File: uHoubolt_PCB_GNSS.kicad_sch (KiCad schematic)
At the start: 88 parts, among them J1 Power In, J12 MMCX-J-P-H-RA-SM1, J2 Debug, J3 Debug, J4 CAN1, J5 CAN2, J6 CAN1, J7 CAN2, Q1 SISA88DN or similar, U1 SAM-M8Q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

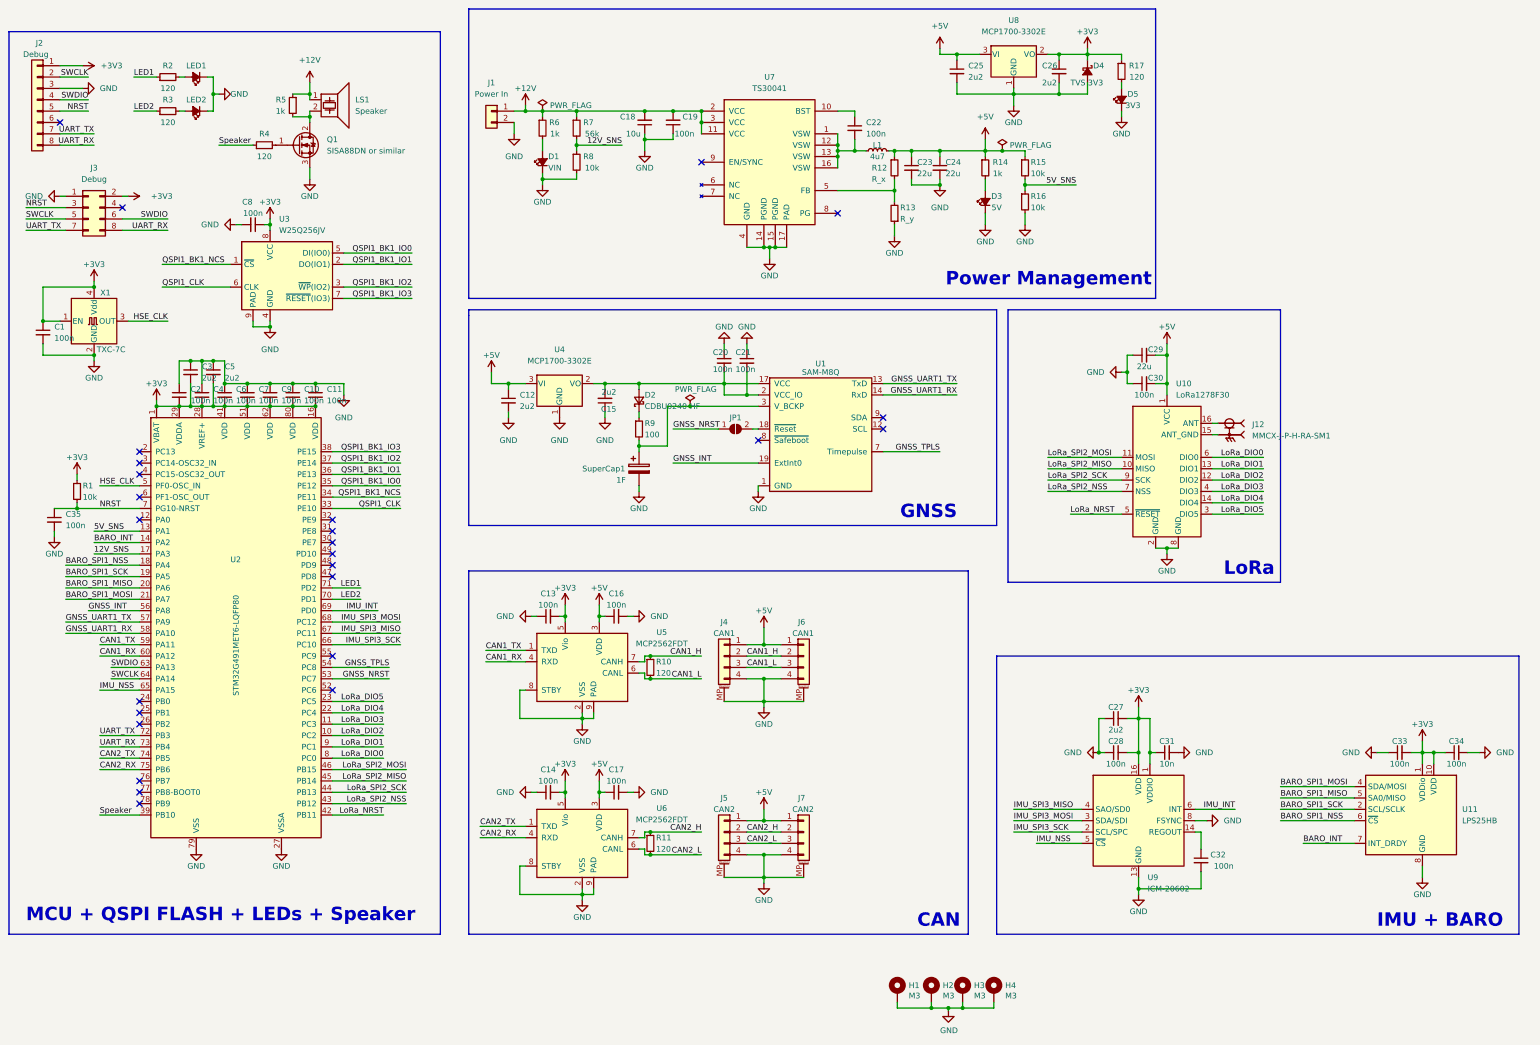
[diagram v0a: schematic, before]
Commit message: Rounded board; updated LoRa module; Small bugfixes and rewiring
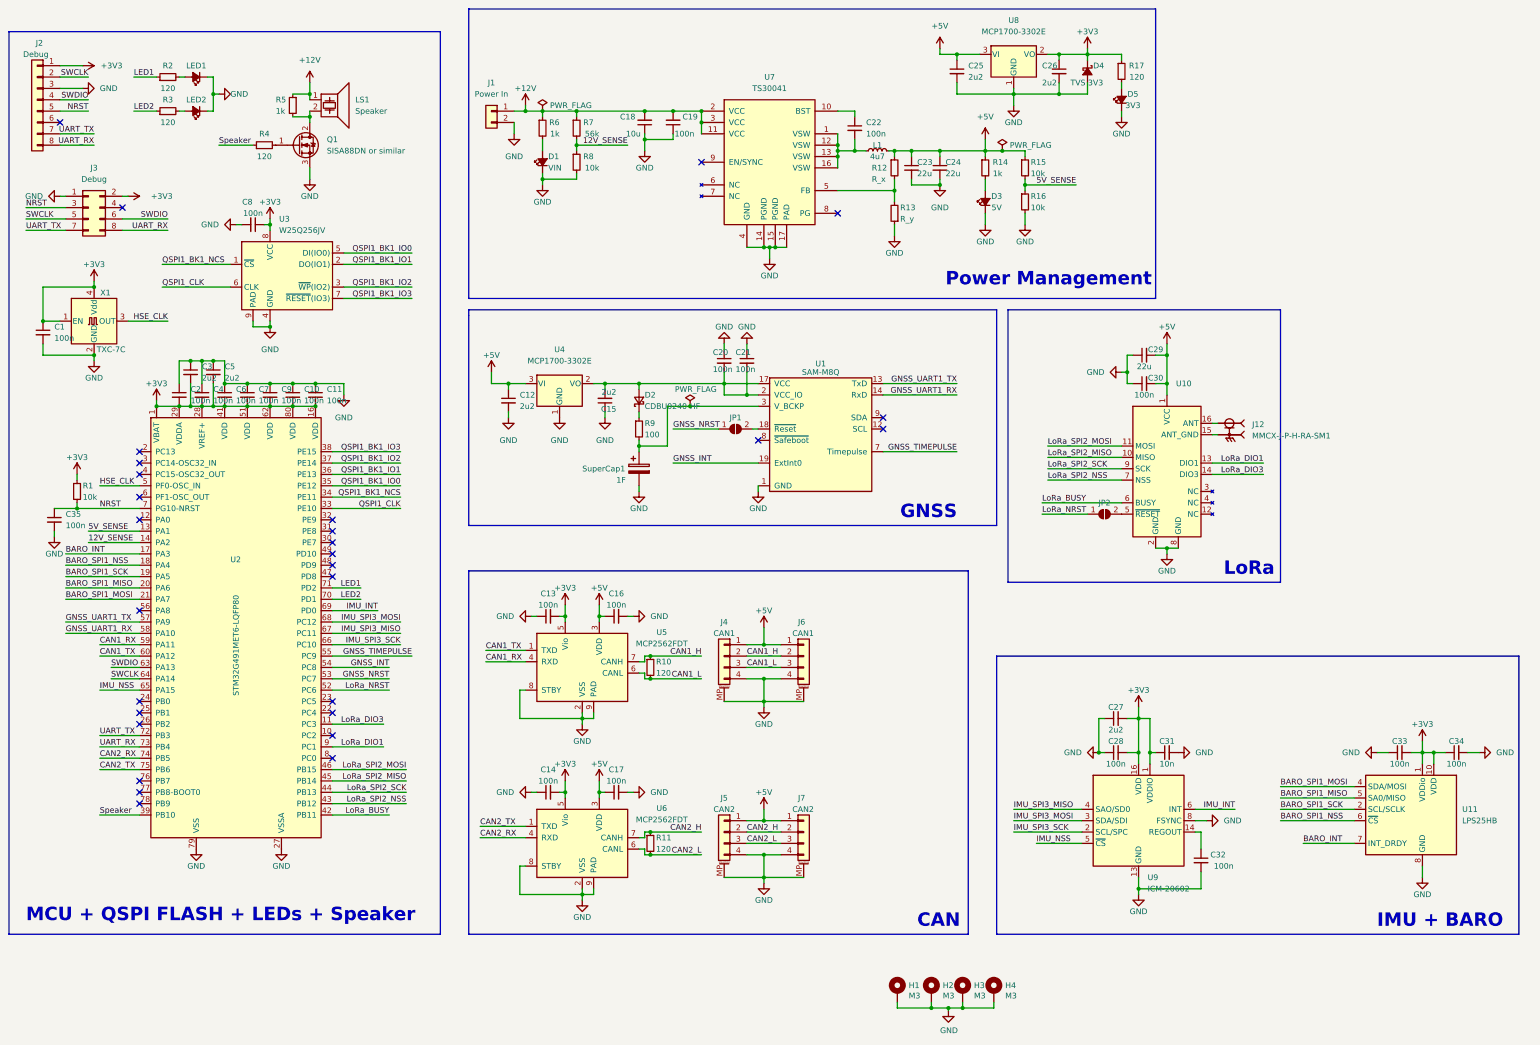
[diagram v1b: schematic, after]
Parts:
- removed U10: LoRa1278F30, TXV_Library_Footprints:G-NiceRF-LoRa1278F30, symbol TXV_Library_Symbols:LoRa1278F30
- added JP2: (no value), symbol Jumper:SolderJumper_2_Open
- added U10: (no value), symbol TXV_Library_Symbols:LoRa1276F30
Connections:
- net +5V: now also U10.1 (VCC)
- net BARO_INT: now also U2.17 (PA3); no longer U2.14 (PA2)
- net CAN1_RX: now also U2.59 (PA11); no longer U2.60 (PA12)
- net CAN1_TX: now also U2.60 (PA12); no longer U2.59 (PA11)
- net CAN2_RX: now also U2.74 (PB5); no longer U2.75 (PB6)
- net CAN2_TX: now also U2.75 (PB6); no longer U2.74 (PB5)
- net GND: now also U10.2 (GND), U10.8 (GND)
- net GNSS_INT: now also U2.54 (PC8); no longer U2.56 (PA8)
- net LoRa_DIO1: now also U10.13 (DIO1)
- net LoRa_DIO3: now also U10.14 (DIO3)
- net LoRa_NRST: now also U2.52 (PC6), JP2.1 (A); no longer U2.42 (PB11)
- net LoRa_SPI2_MISO: now also U10.10 (MISO)
- net LoRa_SPI2_MOSI: now also U10.11 (MOSI)
- net LoRa_SPI2_NSS: now also U10.7 (NSS)
- net LoRa_SPI2_SCK: now also U10.9 (SCK)
- net at J12.S1, J12.S2, J12.S3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: now also U10.15 (ANT_GND)
- net at J12.1: now also U10.16 (ANT)
- net GNSS_TIMEPULSE: now reaches U2.55 (PC9)
- net GNSS_TIMEPULSE: now also U1.7 (Timepulse)
- net 12V_SNS renamed 12V_SENSE
- net 12V_SENSE: now also U2.14 (PA2); no longer U2.17 (PA3)
- net 5V_SNS renamed 5V_SENSE
- removed net GNSS_TPLS: U1.7 (Timepulse), U2.54 (PC8)
- net LoRa_DIO0: no longer names the net of U2.8 (PC0)
- net LoRa_DIO2: no longer names the net of U2.10 (PC2)
- net LoRa_DIO4: no longer names the net of U2.22 (PC4)
- net LoRa_DIO5: no longer names the net of U2.23 (PC5)
- new net: JP2.2 (B), U10.5 (~{RESET})
- new net LoRa_BUSY: U10.6 (BUSY), U2.42 (PB11)
- no-connect marks 26 -> 29

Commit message: Changed MMCX Footprint, Moved mounting holes, moved prog connectors
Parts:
- J12: footprint SAMTEC_MMCX-J-P-H-RA-SM1 -> TXV_Library_Footprints:MMCX_Horizontal_THT; MANUFACTURER Samtec -> (none); MAXIMUM_PACKAGE_HEIGHT 4.6mm -> (none); STANDARD Manufacturer Recommendations -> (none)
- JP2: value (none) -> SolderJumper_; footprint (none) -> Jumper:SolderJumper-2_P1.3mm_Open_Pad1.0x1.5mm
- U10: value (none) -> LoRa1276F30; footprint (none) -> TXV_Library_Footprints:G-NiceRF-LoRa1268F30
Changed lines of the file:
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@@
       (effects (font (size 1.27 1.27)) (justify right))
     )
-    (property "Footprint" "SAMTEC_MMCX-J-P-H-RA-SM1" (id 2) (at 340.36 138.43 0)
+    (property "Footprint" "TXV_Library_Footprints:MMCX_Horizontal_THT" (id 2) (at 340.36 138.43 0)
       (effects (font (size 1.27 1.27)) (justify left bottom) hide)
     )
@@
       (effects (font (size 1.27 1.27)) (justify left bottom) hide)
     )
-    (property "STANDARD" "Manufacturer Recommendations" (id 4) (at 340.36 138.43 0)
+    (property "STANDARD" "" (id 4) (at 340.36 138.43 0)
       (effects (font (size 1.27 1.27)) (justify left bottom) hide)
     )
-    (property "MANUFACTURER" "Samtec" (id 5) (at 340.36 138.43 0)
+    (property "MANUFACTURER" "" (id 5) (at 340.36 138.43 0)
       (effects (font (size 1.27 1.27)) (justify left bottom) hide)
     )
-    (property "MAXIMUM_PACKAGE_HEIGHT" "4.6mm" (id 6) (at 340.36 138.43 0)
+    (property "MAXIMUM_PACKAGE_HEIGHT" "" (id 6) (at 340.36 138.43 0)
       (effects (font (size 1.27 1.27)) (justify left bottom) hide)
     )
@@
       (effects (font (size 1.27 1.27)) (justify left))
     )
-    (property "Value" "" (id 1) (at 328.4094 129.54 0)
-      (effects (font (size 1.27 1.27)) (justify left))
-    )
-    (property "Footprint" "" (id 2) (at 351.79 157.48 0)
+    (property "Value" "LoRa1276F30" (id 1) (at 328.4094 129.54 0)
+      (effects (font (size 1.27 1.27)) (justify left))
+    )
+    (property "Footprint" "TXV_Library_Footprints:G-NiceRF-LoRa1268F30" (id 2) (at 351.79 157.48 0)
       (effects (font (size 1.27 1.27)) hide)
     )
@@
     (pin "1")
   )
-  (symbol (lib_name "W25Q256JV_1") (lib_id "TXV_Library_Symbols:W25Q256JV") (at 129.54 102.87 0) (unit 1)
+  (symbol (lib_id "TXV_Library_Symbols:W25Q256JV") (at 129.54 102.87 0) (unit 1)
     (in_bom yes) (on_board yes) (fields_autoplaced)
     (property "Reference" "U3" (id 0) (at 127.7494 90.17 0)
@@
     (in_bom yes) (on_board yes)
     (property "Reference" "JP2" (id 0) (at 312.42 153.67 0))
-    (property "Value" "" (id 1) (at 313.69 158.75 0)
-      (effects (font (size 1.27 1.27)) hide)
-    )
-    (property "Footprint" "" (id 2) (at 312.42 156.21 0)
+    (property "Value" "SolderJumper_" (id 1) (at 313.69 158.75 0)
+      (effects (font (size 1.27 1.27)) hide)
+    )
+    (property "Footprint" "Jumper:SolderJumper-2_P1.3mm_Open_Pad1.0x1.5mm" (id 2) (at 312.42 156.21 0)
       (effects (font (size 1.27 1.27)) hide)
     )
@@
     )
     (path "/0a145c8e-bbbc-4d52-9317-22af3e6c70bb"
-      (reference "J12") (unit 1) (value "MMCX-J-P-H-RA-SM1") (footprint "SAMTEC_MMCX-J-P-H-RA-SM1")
+      (reference "J12") (unit 1) (value "MMCX-J-P-H-RA-SM1") (footprint "TXV_Library_Footprints:MMCX_Horizontal_THT")
     )
     (path "/49ed1b2c-f59c-4301-915f-8726375c11ed"
